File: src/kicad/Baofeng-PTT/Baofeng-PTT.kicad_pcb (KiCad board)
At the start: 2 copper layers, 18 parts, among them J1 AI, J2 AO, J3 Conn_01x02_Male, J4 PTT, J5 Conn_01x02_Male, J6 Conn_01x02_Male, J7 Conn_01x02_Male, J8 Baofeng, U1 ULN2003

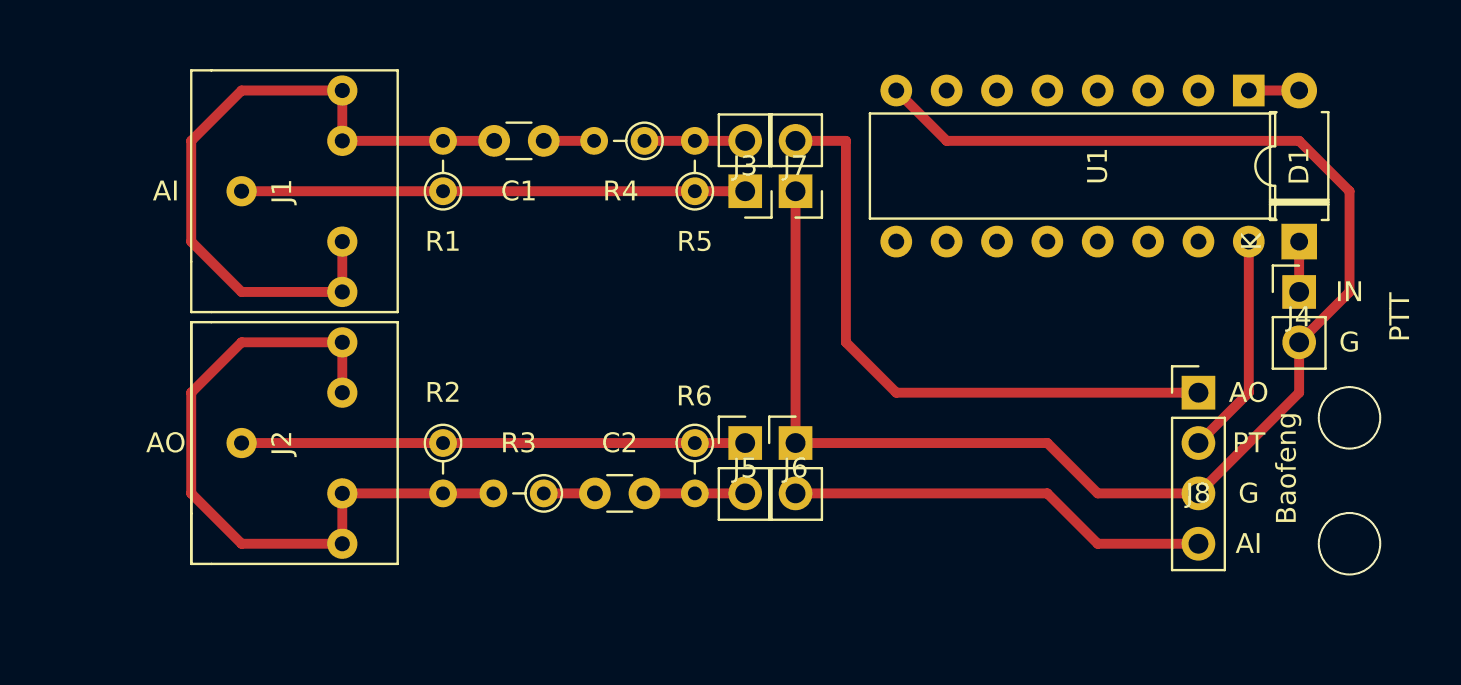
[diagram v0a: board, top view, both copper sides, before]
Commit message: Next version of pcb
Reduce size of pcb
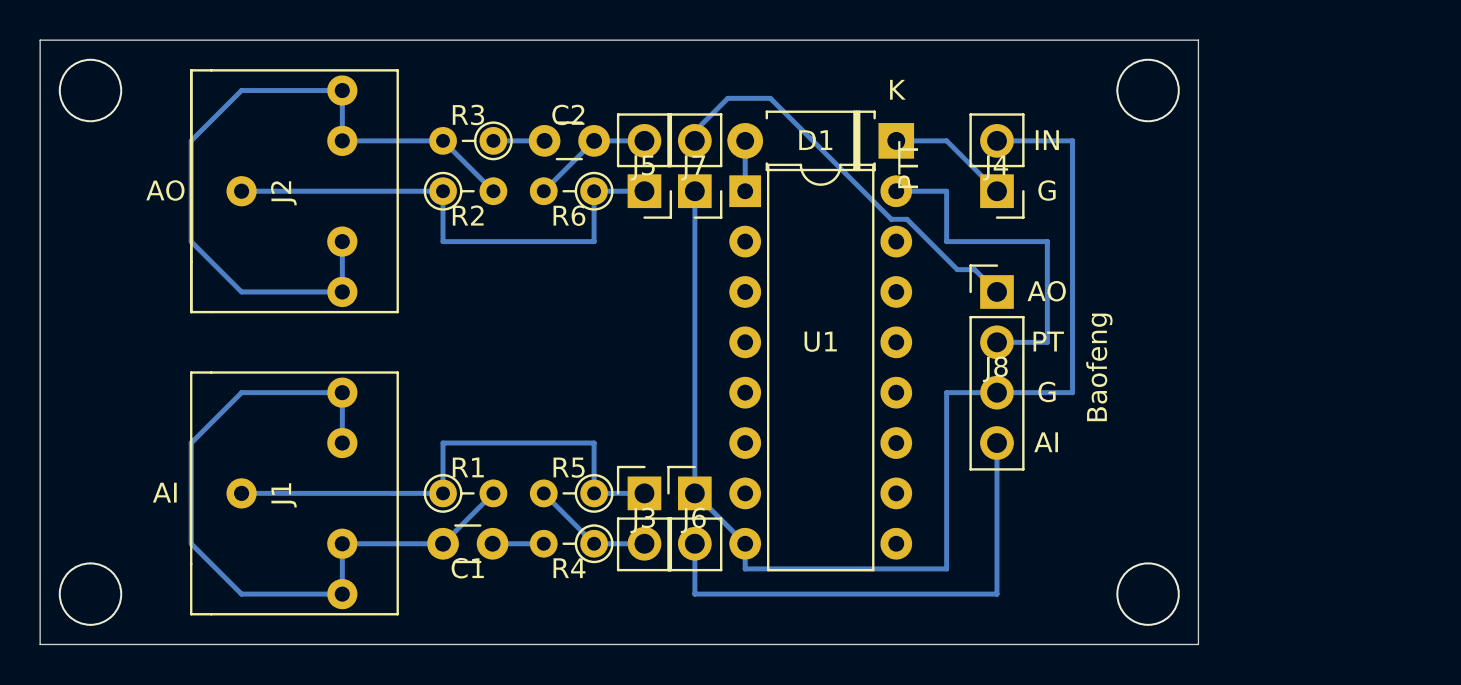
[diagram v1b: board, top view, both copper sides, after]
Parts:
- moved U1 25.9 mm to (200.7, 27.9), turned to 0 degrees
- moved D1 20.9 mm to (208.3, 25.4), turned to 180 degrees
- moved C1 20.5 mm to (187.9, 45.7)
- moved R4 20.5 mm to (193.0, 45.7)
- moved C2 18.0 mm to (193.0, 25.4)
- moved R3 18.0 mm to (188.0, 25.4)
- moved R5 16.1 mm to (193.0, 43.2), turned to 180 degrees
- moved J3 16.1 mm to (195.6, 43.2), turned to 0 degrees
- moved J4 16.1 mm to (213.4, 27.9), turned to 180 degrees
- moved J1 15.2 mm to (177.8, 43.2)
- moved R1 15.2 mm to (185.4, 43.2), turned to 0 degrees
- moved R6 13.7 mm to (193.0, 27.9), turned to 180 degrees
- moved J5 13.7 mm to (195.6, 27.9), turned to 180 degrees
- moved J2 12.7 mm to (177.8, 27.9)
- moved R2 12.7 mm to (185.4, 27.9), turned to 0 degrees
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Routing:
- net GND: track 77.4 -> 62.0 mm
- net AO: track 31.5 -> 20.5 mm
- net PT: track 11.2 -> 17.8 mm
- net AI: track 21.4 -> 25.4 mm
- net Net-(D1-Pad1): track 2.54 -> 6.13 mm
- net Net-(C2-Pad1): track 5.08 -> 6.13 mm
- net Net-(J3-Pad2): track 5.08 -> 6.13 mm
- net Net-(J2-PadR): track 35.1 -> 36.2 mm
- net Net-(C1-Pad2): track 35.2 -> 36.2 mm
- net (no net): vias 2 -> 4
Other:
- board outline added: 58.4 x 30.5 mm
